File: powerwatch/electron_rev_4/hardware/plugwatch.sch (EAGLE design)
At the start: 125 parts, among them J1 DM3AT-SF-PEJM5, J2 TC2030-JLINK-NL, Q1 SI223DDS, U1 BGA725L6-ALT, U10 SIP32510, U11 SIP32510, U12 SIP32510, U13 SIP32510, U14 MPU-9250, U16 MAX6746, U2 SAFFB1G56KB0F0A, U3 ISL29035, U4 MAX-M8, U5 MAX740XESA, U6 SIP32510, U7 NRF51822QF, U8 OPA322AIDBVT, U9 SIP32510, X1 32.768k, X2 16MHz

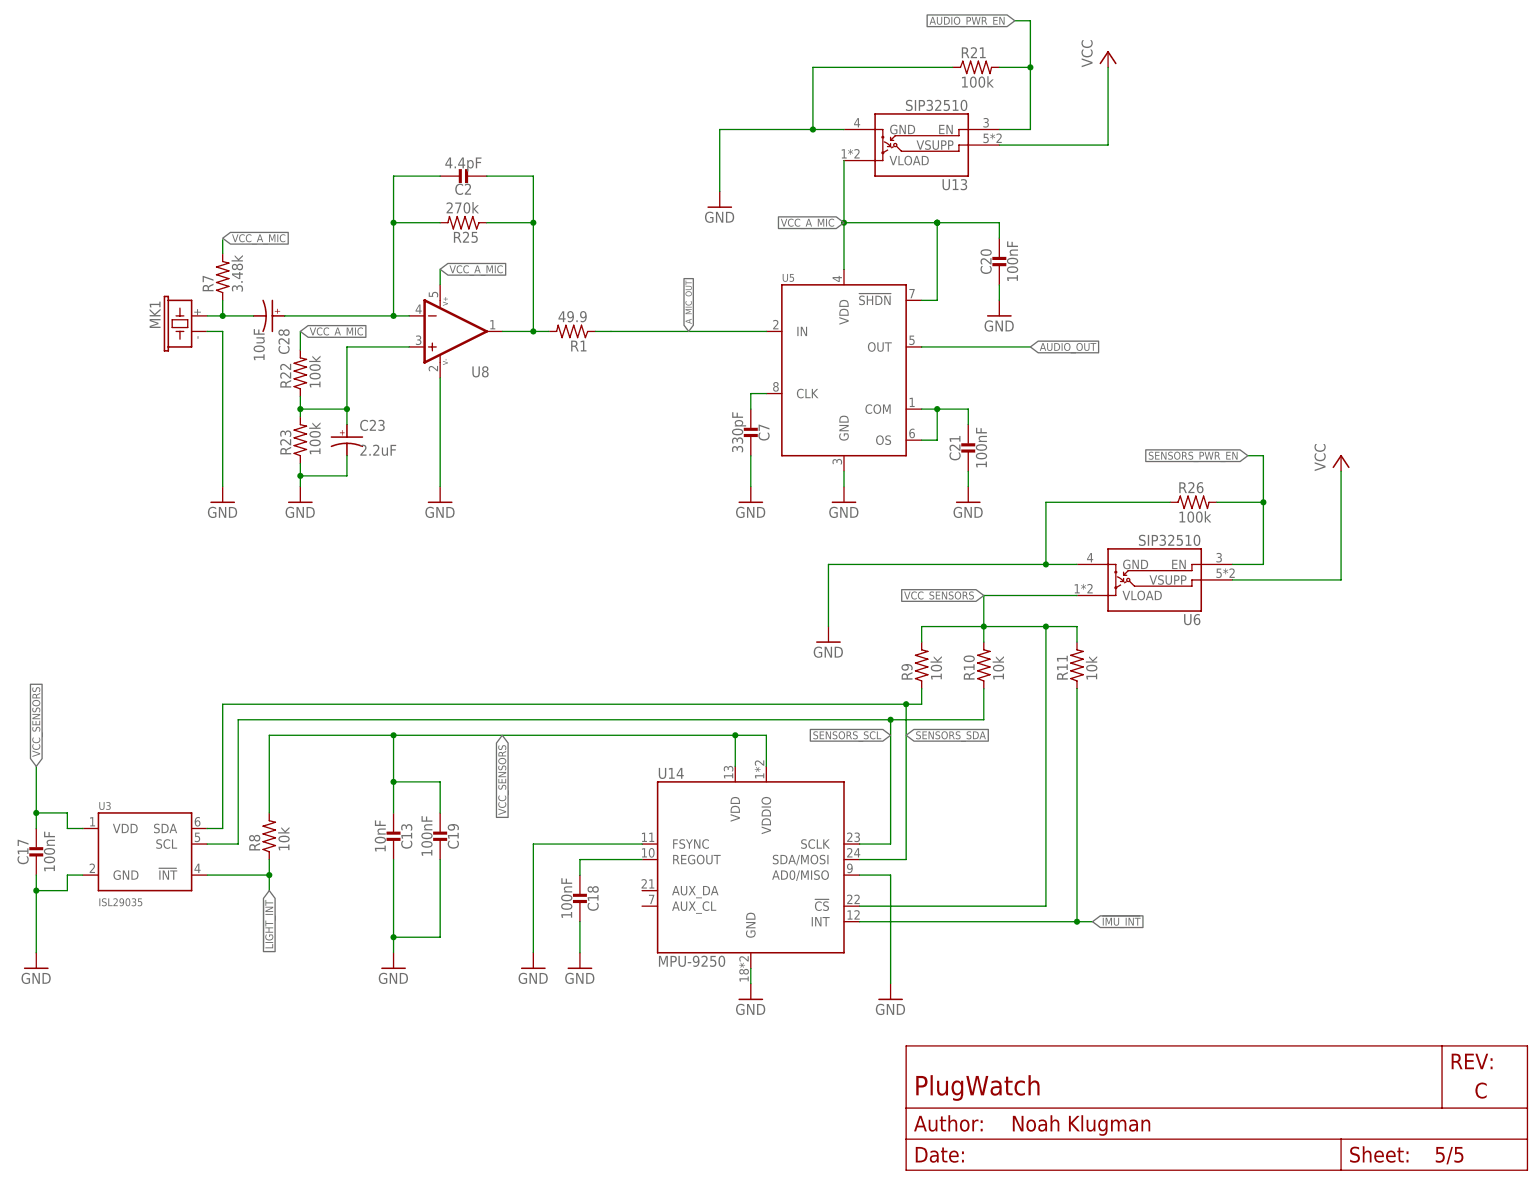
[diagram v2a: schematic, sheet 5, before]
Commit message: add new power supply with updated board shape
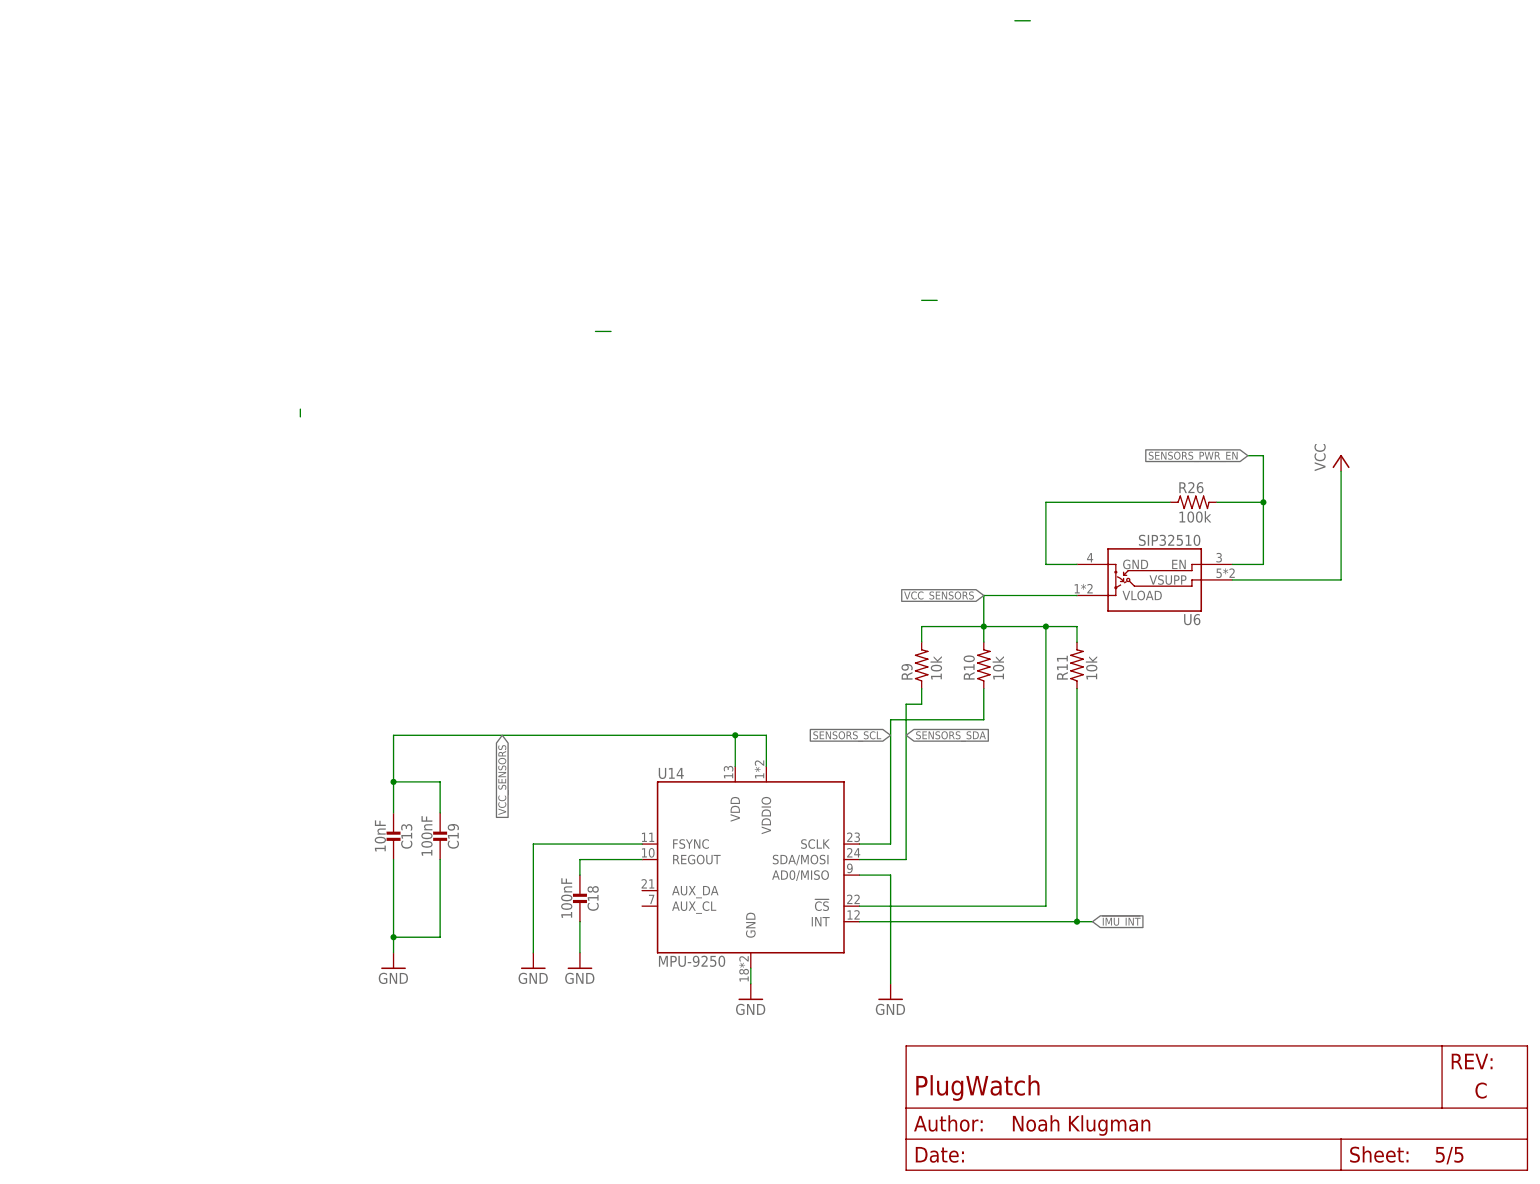
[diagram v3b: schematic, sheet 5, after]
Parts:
- removed C17, C20, C21: 100nF, passives:CAPACITOR0402_CAP
- removed C2: 4.4pF, passives:CAPACITOR0603_CAP
- removed C23: 2.2uF, passives:CAP_POL1206
- removed C28: 10uF, passives:CAP_POL1206
- removed C7: 330pF, passives:CAPACITOR0402_CAP
- removed MK1: AOM-4546P-R, microphones:AOM-4546P-R
- removed R1: 49.9, passives:RESISTOR0603_RES
- removed R21: 100k, passives:RESISTOR0402_RES
- removed R22, R23: 100k, passives:RESISTOR0603_RES
- removed R25: 270k, passives:RESISTOR0603_RES
- removed R7: 3.48k, passives:RESISTOR0603_RES
- removed R8: 10k, passives:RESISTOR0402_RES
- removed U13: SIP32510, chips:SIP32510
- removed U5: MAX740XESA, chips:MAX740XESA
- removed U8: OPA322AIDBVT, opamps:OPA322AIDBVT
- U3: value ISL29035 -> IRM-03-5V; device chips:ISL29035 -> powerwatch:IRM-03-5V
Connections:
- removed net -AMP: C2.1, C28.CATHODE, R25.2, U8.-IN
- removed net N$11: C21.1, U5.COM, U5.OS
- removed net N$4: C28.ANODE, MK1.1, R7.1
- removed net N$5: C2.2, R1.2, R25.1, U8.OUT
- removed net N$6: C7.2, U5.CLK
- removed net N$7: R1.1
- removed net N$9: C23.CATHODE, R22.1, R23.2, U8.+IN
- removed net VCC_A_MIC: C20.1, R22.2, R7.2, U13.VLOAD, U5.!SHDN, U5.VDD, U8.V+
- new net N$30: R26.1, U6.GND
- net !LIGHT_INT: no longer R8.1, U3.!INT
- net AUDIO_OUT: no longer U5.OUT
- net AUDIO_PWR_EN: no longer R21.2, U13.EN
- net A_MIC_OUT: no longer U5.IN
- net GND: no longer C17.2, C20.2, C21.2, C23.ANODE, C7.1, MK1.2, R21.1, R23.1, R26.1, U13.GND, U3.GND, U5.GND, U6.GND, U8.V-
- net SENSORS_SCL: no longer U3.SCL
- net SENSORS_SDA: no longer U3.SDA
- net VCC: no longer U13.VSUPP
- net VCC_SENSORS: no longer C17.1, R8.2, U3.VDD
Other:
- note removed: "Analog Microphone"
- note removed: "I2C Address: 0x44"
- note removed: "Light Sensor"
- note removed: "XXX: Check PCB layout section of TI doc"
- note removed: "http://www.ti.com/lit/ug/tidu765/tidu765.pdf"

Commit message: added AC voltage sense and perturb/observe cap sensing
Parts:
- added AC/L, AC/N: TEST_POINT_0.060IN, headers:TEST_POINT_0.060IN
- added C100, C101: 0.1uF, passives:CAPACITOR0603_CAP
- added C17, C7: 100uF, passives:CAPACITOR1210_CAP
- added C2: 2000uF, rcl:CPOL-USE5-13
- added D10, D11, D8, D9: (no value), passives:DIODE_SCHOTTKYSOD323
- added D4, D5, D6, D7: 3.3V, passives:DIODE_ZENERSOT323
- added F1: 300VAC - 500ma, powerwatch:MICRO_FUSE500MA_350VAC
- added Q2: MOSFET-NCHANNELSMD, fets:MOSFET-NCHANNELSMD
- added R1: 100, passives:RESISTOR0402_RES
- added R21, R30, R31, R8: 750k, passives:RESISTOR0402_RES
- added R22, R25: 1M 1%, rcl:R-US_R0402
- added R23, R28: 1M 1%, rcl:R-US_R0402_SM
- added R7: S14K385, varistor:S14K385
- added RF, RF1: 4.99k 1%, rcl:R-US_R0402
- added RI1, RI2, RI3, RI4: 953k 1%, rcl:R-US_R0402
- added U5, U8: MAX9910, powerfilm:MAX9910
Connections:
- new net 5V: ASSY1.VIN, C17.1, C2.+, C7.1, R1.1, U3.V+
- new net AC/L-FUSED: F1.P$2, R30.1, R7.1, R8.1, RI1.1, U3.AC/L
- new net AC/L-MEASURE: D6.CATHODE, D8.CATHODE, R30.2
- new net AC/L-PERTURB: D4.CATHODE, D9.CATHODE, R8.2
- new net AC/L-SENSE: RF.2, U5.OUT
- new net AC/N-FUSED: AC/N.TESTPOINT, R21.1, R31.1, R7.2, RI3.1, U3.AC/N
- new net AC/N-MEASURE: D10.CATHODE, D5.CATHODE, R31.2
- new net AC/N-PERTURB: D11.CATHODE, D7.CATHODE, R21.2
- new net AC/N-SENSE: RF1.2, U8.OUT
- new net N$32: Q2.G, R1.2
- new net N$38: AC/L.TESTPOINT, F1.P$1
- new net N$42: R22.1, R23.2, U5.IN+
- new net N$43: RF.1, RI1.2, RI2.2, U5.IN-
- new net N$44: R25.1, R28.2, U8.IN+
- new net N$45: RF1.1, RI3.2, RI4.2, U8.IN-
- new net N$9: C17.2, C2.-, C7.2, Q2.D, U3.V-
- net GND: now also C100.2, C101.2, D10.ANODE, D11.ANODE, D4.ANODE, D5.ANODE, D6.ANODE, D7.ANODE, D8.ANODE, D9.ANODE, Q2.S, R23.1, R28.1, RI2.1, RI4.1, U5.VSS, U8.VSS
- net VCC: now also C100.1, C101.1, R22.2, R25.2, U5.VCC, U8.VCC
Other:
- note added: "-(RF/RI)*VTEST + VCC/2"
- note added: "Assuming 340Vpp, a 750k resistor will dissipate 0.15W, and a 3.3v zener will dissipate 1.4mW"
- note added: "Output voltage:"
- note added: "The peak power is 2A * 600uS = ~4.5mJ. We are adding 8mJ of energy buffer to be safe. 8mJ of energy with a 5V to 4V swing is about 2mF"
- note added: "The schottkey diode is necessary to protect the MCU pin against the -0.7-1V potentially caused by the zener forward voltage if AC/L or AC/N are negative relative to GND. The schottkey has Vf < 0.3 which is less than the internal diodes on most MCUs."
- note added: "This circuit handles up to 340V with a 3.3V reference."
- note added: "This mosfet should turn on when power is supplied by the circuit - otherwise we float GND for capacitance measurement."
- note added: "This will protect the sampling circuit against surges"
- note added: "We use a seperate AC Measure pin so that we can more directly sense the perturbation by the digital output. The full-scale voltage sensing circuit (below) could also be used, but would only sense <1% of its dynamic range."
- note removed: "Power Management"

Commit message: add rtc and descriptions, remove BLE
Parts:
- removed A1: ANT3216A063R2400A, chips:ANT3216A063R2400A
- removed B1: BAL-NRF01D3, chips:BAL-NRF01D3
- removed C10: 2.2nF, passives:CAPACITOR0402_CAP
- removed C14: 47nF, passives:CAPACITOR0402_CAP
- removed C16: 100nF, passives:CAPACITOR0402_CAP
- removed C22: 1uF, passives:CAPACITOR0402_CAP
- removed C25: 4.7uF, passives:CAPACITOR0402_CAP
- removed C4, C5, C6: 12pF, passives:CAPACITOR0402_CAP
- removed C8, C9: 1nF, passives:CAPACITOR0402_CAP
- removed D2: BLUE, leds:LED0603
- removed J2: TC2030-JLINK-NL, connector:TC2030-JLINK-NL
- removed L2: 15nH, passives:INDUCTOR0402
- removed L3: 10uH, passives:INDUCTOR0603
- removed S1: B3U-1000P, switches:B3U-1000P
- removed TP10, TP11, TP25, TP27, TP7, TP9: TEST_POINT_0.040IN, headers:TEST_POINT_0.040IN
- removed U11: SIP32510, chips:SIP32510
- removed U7: NRF51822QF, chips:NRF51822QF
- removed X2: 16MHz, crystals:TXC-8Y
- added B2: (no value), batteries:MS518SE
- added R32, R33: 1.5k, passives:RESISTOR0402_RES
- added R34: 10k, passives:RESISTOR0402_RES
- added U13: AB1815-T3, chips:AB1815-T3
- C1: value 0.8pF -> 1uF; device passives:CAPACITOR0402_CAP -> passives:CAPACITOR0603_CAP; DESCRIPTION CAP CER 0.8PF 50V C0G/NP0 0402 -> (none); DIGIKEY 490-6269-1-ND -> (none); MANUFACTURER Murata -> (none); MPN GRM1555C1HR80BA01D -> (none)
- C3: value 12pF -> 47pF; device passives:CAPACITOR0402_CAP -> passives:CAPACITOR0603_CAP; DESCRIPTION CAP CER 12PF 50V C0G/NP0 0402 -> (none); DIGIKEY 490-6197-1-ND -> (none); MANUFACTURER Murata -> (none); MPN GRM1555C1H120GA01D -> (none)
- R15: value 12k -> 100k; DESCRIPTION RES SMD 12K OHM 1% 1/16W 0402 -> RES SMD 150 OHM 1% 1/16W 0402; DIGIKEY RMCF0402FT12K0CT-ND -> RMCF0402FT150RCT-ND; MPN RMCF0402FT12K0 -> RMCF0402FT150R
- R2: value 150 -> 10k
- R20: value 100k -> 10k; DESCRIPTION RES SMD 100K OHM 1% 1/16W 0402 -> RES SMD 150 OHM 1% 1/16W 0402; DIGIKEY 1276-3432-1-ND -> RMCF0402FT150RCT-ND; MANUFACTURER Samsung -> Stackpole Electronics; MPN RC1005F104CS -> RMCF0402FT150R
- R5: value 1k -> 100k; DESCRIPTION RES SMD 1K OHM 1% 1/16W 0402 -> RES SMD 150 OHM 1% 1/16W 0402; DIGIKEY RMCF0402FT1K00CT-ND -> RMCF0402FT150RCT-ND; MPN RMCF0402FT1K00 -> RMCF0402FT150R
- X1: value 32.768k -> ABS07-32.768KHZ-7-T; device crystals:ABS05-32.768KHZ-9-T -> crystals:ABS07-32.768KHZ-7-T
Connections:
- removed net !LIGHT_INT: ASSY1.A1, TP7.TESTPOINT
- removed net AUDIO_OUT: ASSY1.B2, TP11.TESTPOINT
- removed net AUDIO_PWR_EN: ASSY1.B4, TP10.TESTPOINT
- removed net AVDD1: C22.1, C8.1, L2.1, U7.AVDD
- removed net A_MIC_OUT: TP27.TESTPOINT
- removed net DCC1: L3.2, U7.DCC
- removed net N$10: B1.ANT1, U7.ANT1
- removed net N$12: B1.ANT2, U7.ANT2
- removed net N$15: L2.2, L3.1
- removed net N$22: C9.1, U7.DEC1
- removed net N$24: C14.1, U7.DEC2
- removed net N$26: R2.2, S1.P$2
- removed net NRF_A2: C6.1, U7.P27/AIN1/XL1, X1.2
- removed net NRF_A3: C5.1, U7.P26/AIN0/XL2, X1.1
- removed net NRF_P29: D2.CATHODE, U7.P29
- removed net NRF_SWDCLK: J2.SWDCLK, R15.1, U7.SWDCLK
- removed net NRF_SWDIO/!RESET: ASSY1.D7, J2.SWDIO, R2.1, TP25.TESTPOINT, U7.SWDIO/!RESET
- removed net VCC_BLE: C16.1, C25.1, J2.VCC, R5.1, U11.VLOAD, U7.VDD
- removed net VDD_PA1: B1.VDD_PA, C10.1, U7.VDD_PA
- new net !RTC_CS: U13.!CS
- new net !RTC_INT1: R34.2, U13.FOUT/!IRQ1
- new net !RTC_INT2: R20.2, U13.!IRQ2
- new net N$4: B2.+, R32.2, R33.1
- new net N$5: R33.2, U13.VBAT
- net 5V: now also R5.1
- net BLE_PWR_EN: no longer R20.2, TP9.TESTPOINT, U11.EN
- net BLE_RXD: no longer ASSY1.C3, U7.P17
- net BLE_TXD: no longer ASSY1.C2, U7.P16
- net GND: now also B2.-, R2.2, U13.!EXTR, U13.VSS; no longer A1.GND, B1.GND, C10.2, C14.2, C16.2, C22.2, C25.2, C4.2, C5.2, C6.2, C8.2, C9.2, J2.GND, R20.1, S1.P$1, U11.GND, U7.GND
- net N$13: now also C3.1, U13.AF; no longer A1.ANTENNA, B1.SE, C1.1
- net N$20: now also U13.XO, X1.2; no longer C3.1, U7.XC1, X2.1
- net N$21: now also U13.XI, X1.1; no longer C4.1, U7.XC2, X2.2
- net N$25: now also R15.1, U13.EXTI; no longer D2.ANODE
- net SD_MISO: now also U13.SDO
- net SD_MOSI: now also U13.SDI
- net SD_SCLK: now also U13.SCL
- net VCC: now also C1.1, R20.1, R32.1, R34.1, U13.VCC; no longer U11.VSUPP
- net WDI: now also R2.1, U13.WDI
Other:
- note added: "Battery charges from 3.3v through 1.5k resistor per datasheet."
- note added: "If we dont' have VCC, nothing will be able to read these anyways."
- note added: "Must be less than 2.8v in the case of vbat (2.5v + 0.3v tolerance). Max input thresh is 2.0v, so dividing 5v/2 (2.5v) should work. Note that this is only a problem during transition (5v but no VCC)."
- note added: "Must not float. Could float if particle is sleeping - so pull down."
- note added: "You don't need external caps on this crystal. Verified working on permamote."
- note removed: "BLE Radio"
- note removed: "JTAG Connection"
- note removed: "Note: Pin choices are arbitrary"
- note removed: "Reset Switch"
